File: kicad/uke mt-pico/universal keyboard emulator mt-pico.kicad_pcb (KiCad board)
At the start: 2 copper layers, 42 parts, among them J1 Mode Select, J2 OLED Adapter, J3 Serial, J4 Conn_02x20_Odd_Even, J5 SWD, J6 Pico VBUS, SW1 Reset Pico, U1 MT8816, U2 74HCT245, U3 74HCT245, U4 Pico, U5 74HCT595-VERIFY-FOOTPRINT

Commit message: minor pixel pushing
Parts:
- moved J3 12.8 mm to (166.9, 74.1), turned to 180 degrees
- moved U4 7.83 mm to (185.8, 85.0)
- moved C6 7.21 mm to (205.1, 75.7)
- moved H2 7.21 mm to (209.8, 56.1)
- moved J1 7.21 mm to (204.9, 78.9)
- moved J5 7.21 mm to (165.4, 110.2)
- moved J6 7.21 mm to (205.0, 60.1)
- moved R1 7.21 mm to (205.1, 94.5)
- moved SW1 7.21 mm to (204.5, 89.0)
- moved TP1 7.21 mm to (205.0, 100.9)
- moved TP3 7.21 mm to (205.0, 108.0)
- moved D4 7.21 mm to (205.0, 69.6)
- moved H4 7.21 mm to (210.0, 115.5)
- moved R9 7.21 mm to (204.6, 97.9)
- moved TP2 7.21 mm to (204.9, 104.0)
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
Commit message: Pre-route #1
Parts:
- added TP4: TestPoint, TestPoint:TestPoint_Pad_1.0x1.0mm, F.Cu at (200.5, 68.7)
- added TP5: TestPoint, TestPoint:TestPoint_Pad_1.0x1.0mm, F.Cu at (200.3, 94.0)
- added TP6: TestPoint, TestPoint:TestPoint_Pad_1.0x1.0mm, F.Cu at (200.5, 63.5)
- moved R2 32.1 mm to (149.7, 107.1), turned to -90 degrees
- moved R4 31.8 mm to (155.8, 107.2), turned to -90 degrees
- moved R3 31.3 mm to (161.8, 107.2), turned to -90 degrees
- moved D1 28.9 mm to (147.3, 106.9), turned to -90 degrees
- moved D3 28.4 mm to (153.4, 107.1), turned to -90 degrees
- moved D2 28.4 mm to (159.5, 107.1), turned to -90 degrees
- moved U5 8.70 mm to (156.5, 94.9)
- moved C1 8.70 mm to (156.7, 91.2)
- moved D5 8.70 mm to (156.6, 95.5)
- moved J2 5.52 mm to (152.5, 102.3), turned to 90 degrees
- moved D6 5.18 mm to (156.6, 77.8)
- moved R5 5.18 mm to (156.7, 83.8)
- moved R7 5.18 mm to (156.6, 80.9)
- moved U2 5.18 mm to (156.6, 82.0)
- moved C2 5.18 mm to (157.0, 86.6)
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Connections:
- U4 pad 27: unconnected-(U4-Pad27) -> Net-(U4-Pad27)
- U4 pad 37: unconnected-(U4-Pad37) -> Net-(U4-Pad37)
- U4 pad 39: unconnected-(U4-Pad39) -> Net-(U4-Pad39)

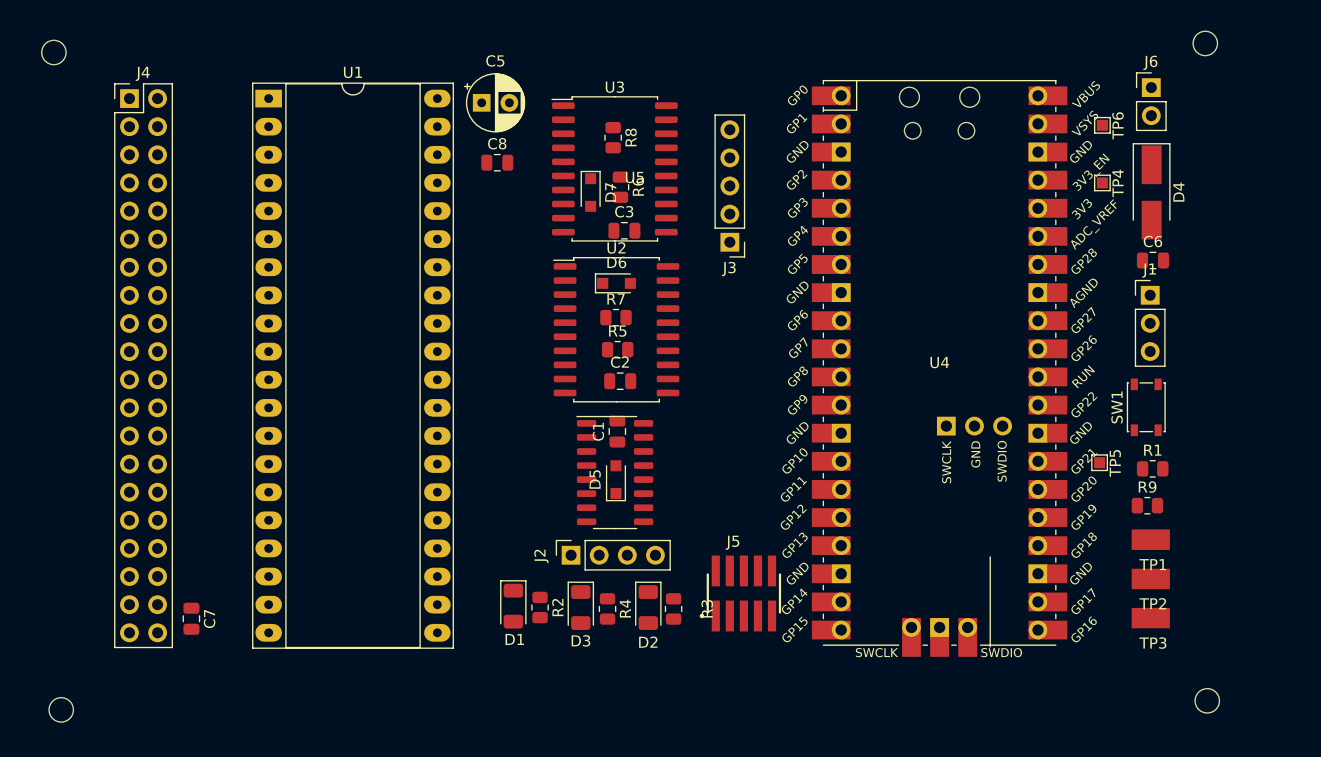
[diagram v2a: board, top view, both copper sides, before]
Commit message: all but 5v routed
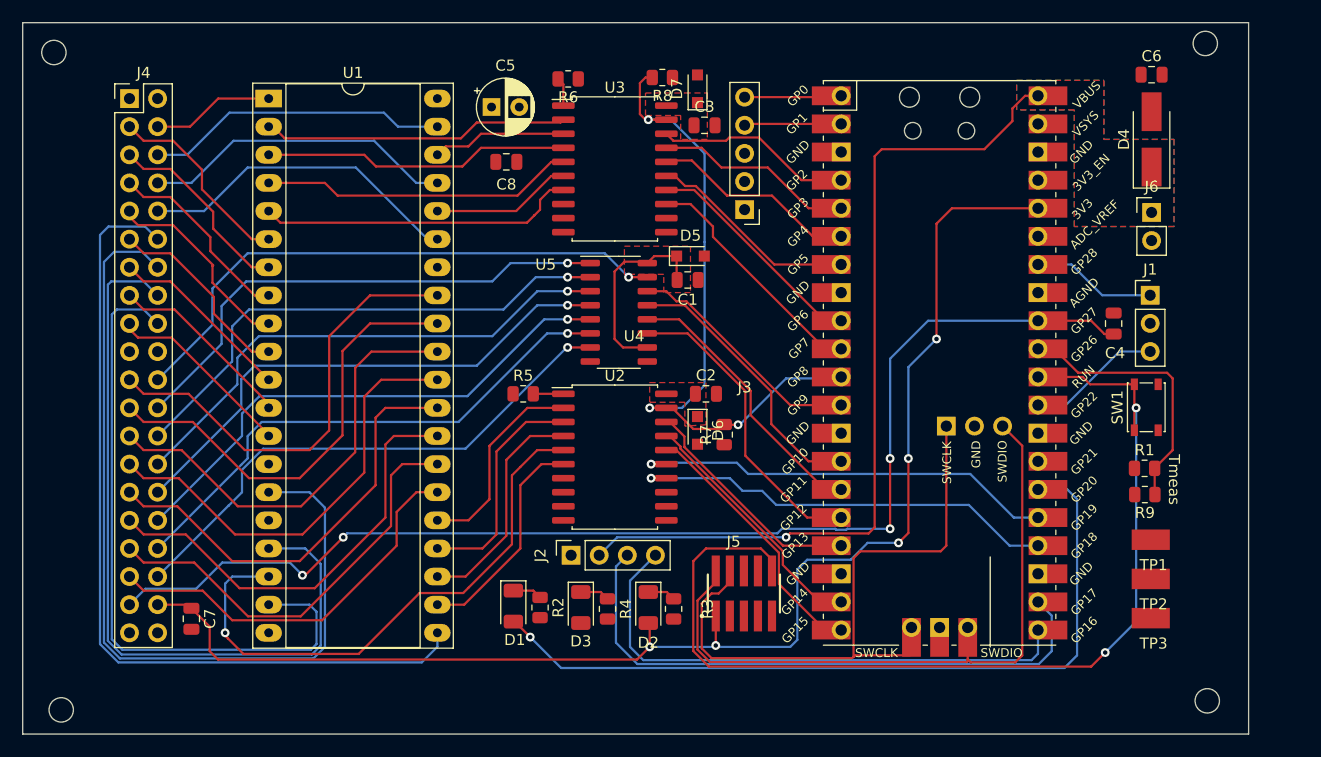
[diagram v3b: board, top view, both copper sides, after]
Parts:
- removed TP4, TP5, TP6: TestPoint, TestPoint:TestPoint_Pad_1.0x1.0mm
- added C4: 100n, Capacitor_SMD:C_0805_2012Metric, F.Cu at (201.5, 81.4)
- moved D5 21.3 mm to (163.3, 75.3), turned to 0 degrees
- moved C6 16.8 mm to (205.0, 58.9)
- moved D6 15.2 mm to (164.0, 91.1), turned to -90 degrees
- moved C1 15.1 mm to (163.1, 77.5), turned to 0 degrees
- moved U5 14.5 mm to (156.8, 80.4)
- moved R7 14.4 mm to (166.4, 91.4), turned to 90 degrees
- moved D7 13.5 mm to (164.0, 60.2), turned to 90 degrees
- moved C3 12.0 mm to (164.6, 63.5)
- moved U2 11.5 mm to (156.5, 93.5)
- moved J6 11.3 mm to (205.0, 71.4)
- moved R6 10.9 mm to (152.3, 59.3), turned to 180 degrees
- moved R5 9.42 mm to (148.2, 87.8)
- moved C2 7.83 mm to (164.7, 87.8)
- moved R8 7.02 mm to (160.8, 59.2), turned to 180 degrees
- moved D4 4.80 mm to (205.0, 64.8), turned to 90 degrees
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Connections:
- C1 pad 1: +5V -> Net-(D5-Pad1)
- C2 pad 1: +5V -> Net-(U2-Pad20)
- C3 pad 1: +5V -> Net-(U3-Pad20)
- D6 pad 1: Net-(D6-Pad1) -> Net-(U2-Pad20)
- J4 pad 10: /ROW3 -> /ROW0
- J4 pad 11: /COL4 -> /COL8
- J4 pad 13: /COL5 -> /COL9
- J4 pad 14: /ROW5 -> /ROW7
- J4 pad 15: /COL6 -> /COL10
- J4 pad 17: /COL7 -> /COL11
- J4 pad 18: /ROW7 -> /ROW5
- J4 pad 21: /COL8 -> /COL0
- J4 pad 23: /COL9 -> /COL1
- J4 pad 25: /COL10 -> /COL2
- J4 pad 27: /COL11 -> /COL3
- J4 pad 29: /COL12 -> /COL4
- J4 pad 3: /COL0 -> /COL14
- J4 pad 31: /COL13 -> /COL5
- J4 pad 33: /COL14 -> /COL12
- J4 pad 35: /COL15 -> /COL13
- J4 pad 4: /ROW0 -> /ROW3
- J4 pad 5: /COL1 -> /COL15
- J4 pad 6: /ROW1 -> /ROW2
- J4 pad 7: /COL2 -> /COL6
- J4 pad 8: /ROW2 -> /ROW1
- J4 pad 9: /COL3 -> /COL7
- U2 pad 11: /rpAY2 -> unconnected-(U2-Pad11)
- U2 pad 12: /rpRESET -> unconnected-(U2-Pad12)
- U2 pad 13: /rpAX3 -> unconnected-(U2-Pad13)
- U2 pad 14: /rpAX0 -> /rpAX1
- U2 pad 15: /rpAY1 -> /rpSTROBE
- U2 pad 16: /rpAY0 -> /rpAX2
- U2 pad 17: /rpAX1 -> /rpAY0
- U2 pad 18: /rpAX2 -> /rpAY1
- U2 pad 2: /AX2 -> /AY1
- U2 pad 20: Net-(D6-Pad1) -> Net-(U2-Pad20)
- U2 pad 3: /AX1 -> /AY0
- U2 pad 4: /AY0 -> /AX2
- U2 pad 5: /AY1 -> /STROBE
- U2 pad 6: /AX0 -> /AX1
- U2 pad 7: /AX3 -> unconnected-(U2-Pad7)
- U2 pad 8: /RESET -> unconnected-(U2-Pad8)
- U2 pad 9: /AY2 -> unconnected-(U2-Pad9)
- U3 pad 11: /rpCS -> unconnected-(U3-Pad11)
- U3 pad 12: /rpDATA -> unconnected-(U3-Pad12)
- U3 pad 13: unconnected-(U3-Pad13) -> /rpAX0
- U3 pad 14: unconnected-(U3-Pad14) -> /rpCS
- U3 pad 15: unconnected-(U3-Pad15) -> /rpAX3
- U3 pad 16: unconnected-(U3-Pad16) -> /rpRESET
- U3 pad 17: /rpSTROBE -> /rpDATA
- U3 pad 18: unconnected-(U3-Pad18) -> /rpAY2
- U3 pad 2: unconnected-(U3-Pad2) -> /AY2
- U3 pad 3: /STROBE -> /DATA
- U3 pad 4: unconnected-(U3-Pad4) -> /RESET
- U3 pad 5: unconnected-(U3-Pad5) -> /AX3
- U3 pad 6: unconnected-(U3-Pad6) -> /CS
- U3 pad 7: unconnected-(U3-Pad7) -> /AX0
- U3 pad 8: /DATA -> unconnected-(U3-Pad8)
- U3 pad 9: /CS -> unconnected-(U3-Pad9)
- U4 pad 10: /595_Latch -> /rpAX0
- U4 pad 12: /rpAX2 -> /595_DATA
- U4 pad 14: /rpAX1 -> /~{595_OE}
- U4 pad 15: /rpAY0 -> /595_Latch
- U4 pad 16: /rpAY1 -> /595_CLK
- U4 pad 17: /rpAX0 -> /rpAY1
- U4 pad 19: /rpAX3 -> /rpAY0
- U4 pad 20: /rpRESET -> /rpAX2
- U4 pad 24: /~{595_OE} -> /rpAX1
- U4 pad 25: /rpAY2 -> /rpSTROBE
- U4 pad 27: Net-(U4-Pad27) -> unconnected-(U4-Pad27)
- U4 pad 37: Net-(U4-Pad37) -> unconnected-(U4-Pad37)
- U4 pad 39: Net-(U4-Pad39) -> unconnected-(U4-Pad39)
- U4 pad 4: /595_DATA -> /rpAY2
- U4 pad 5: /595_CLK -> /rpDATA
- U4 pad 6: /rpCS -> /rpRESET
- U4 pad 7: /rpDATA -> /rpAX3
- U4 pad 9: /rpSTROBE -> /rpCS
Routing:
- net +3V3: track 0.00 -> 123.5 mm, vias 0 -> 5
- net /ADID: track 0.00 -> 110.0 mm, vias 0 -> 4
- net /RUN: track 0.00 -> 92.0 mm, vias 0 -> 2
- net /ROW7: track 0.00 -> 79.4 mm
- net +5VA: track 0.00 -> 77.1 mm, vias 0 -> 1
- net /ROW4: track 0.00 -> 76.0 mm
- net /LED: track 0.00 -> 71.1 mm, vias 0 -> 1
- net /ROW6: track 0.00 -> 70.0 mm
- net /SWDIO: track 0.00 -> 62.5 mm
- net /ROW5: track 0.00 -> 60.8 mm
- net /245s_CE: track 0.00 -> 59.9 mm, vias 0 -> 3
- net /SWCLK: track 0.00 -> 56.2 mm
- net /OLED_SCL: track 0.00 -> 53.9 mm
- net /SH0: track 0.00 -> 51.8 mm, vias 0 -> 1
- net /STROBE: track 0.00 -> 51.4 mm, vias 0 -> 1
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- added copper zone on B.Cu, net +5VA
- added copper zone on F.Cu, net +5VA
- added copper zone on F.Cu, net Net-(D5-Pad1)
- added copper zone on F.Cu, net Net-(U2-Pad20)
- added copper zone on F.Cu, net Net-(U3-Pad20)
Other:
- board outline added: 110.7 x 64.3 mm
- rule pad_to_mask_clearance: 0 -> 0.00254
- board text added: "Tmeas"
